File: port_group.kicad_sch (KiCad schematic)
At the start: 20 parts, among them U2 AOZ1268QI

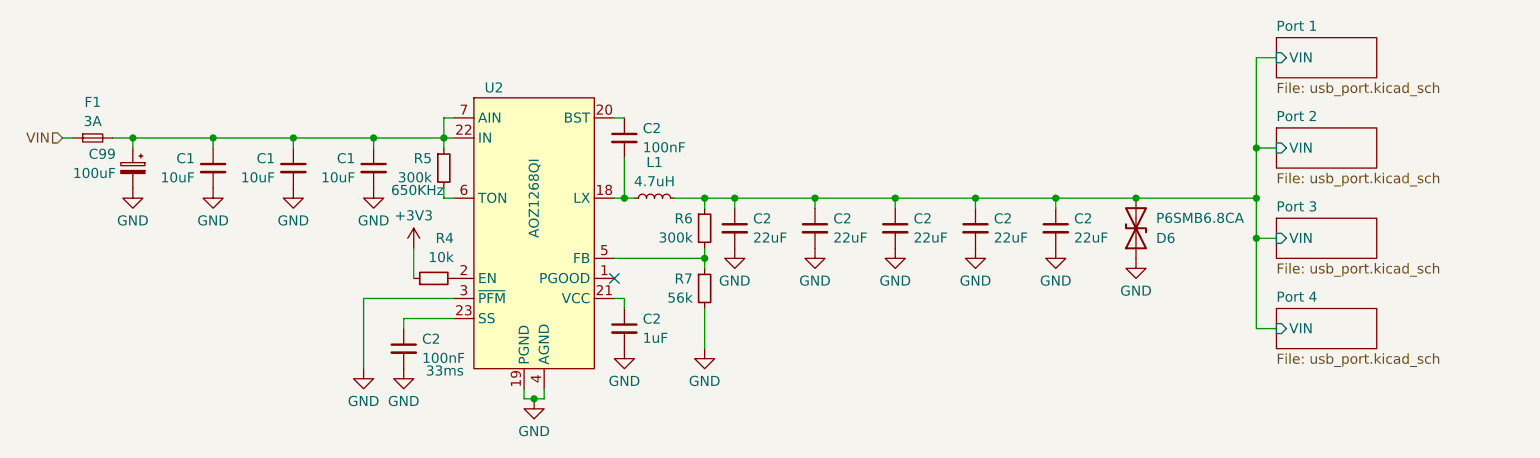
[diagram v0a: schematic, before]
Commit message: Add 5V auxiliary supply
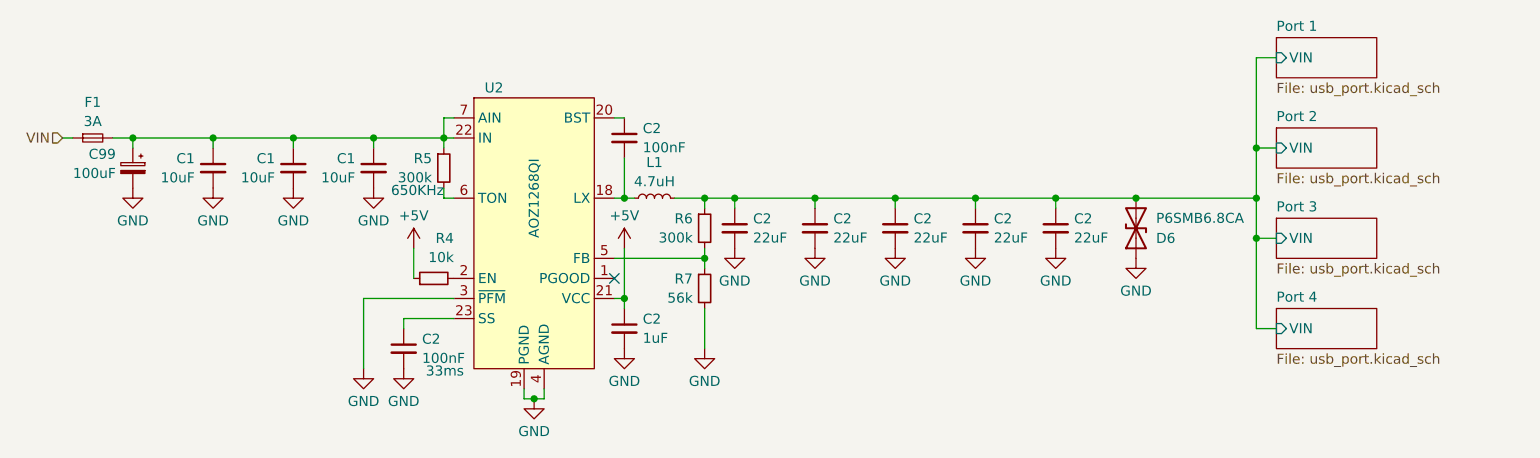
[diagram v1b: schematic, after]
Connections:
- net +3V3 is gone; now on net +5V: R4.1
- net +5V: now reaches C2.1, U2.21 (VCC)

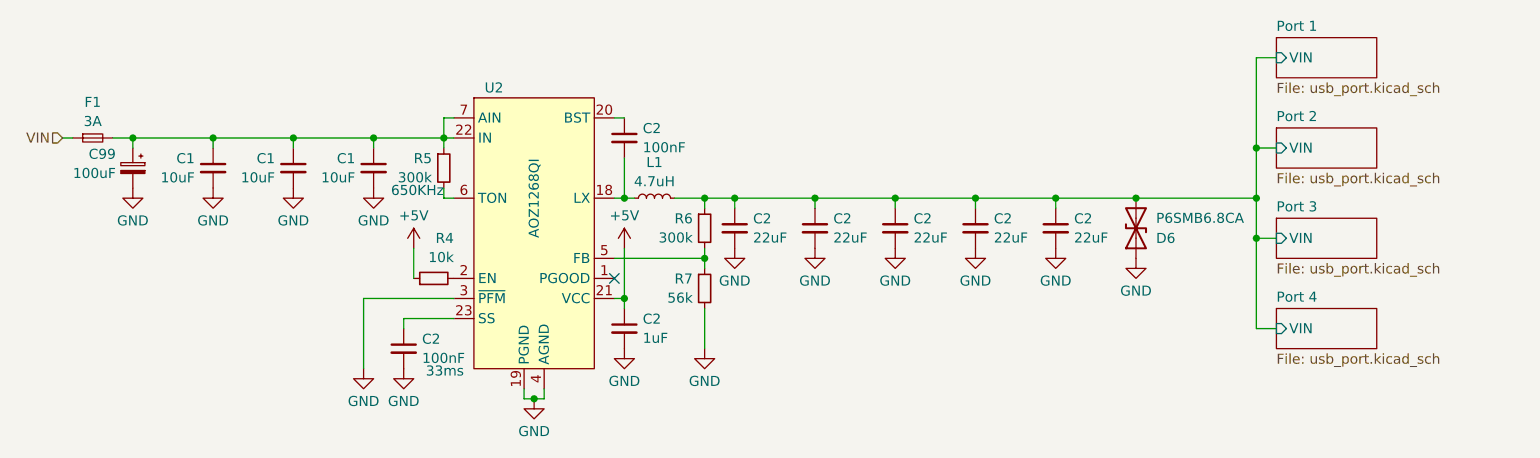
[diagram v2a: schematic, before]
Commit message: Do not populate buck converter VCC jumpers
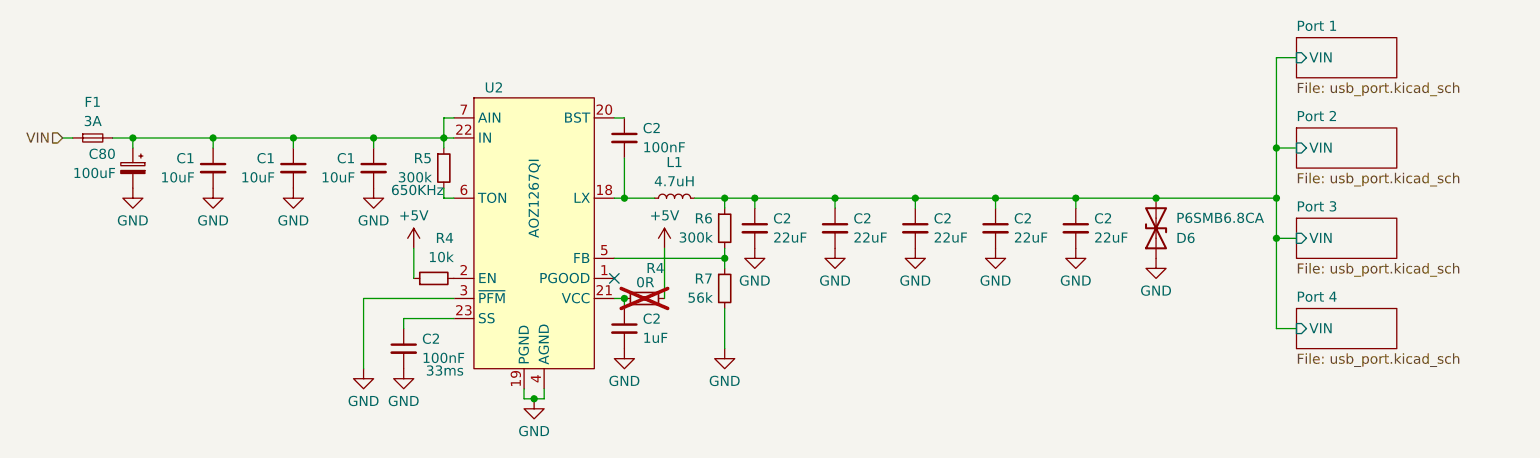
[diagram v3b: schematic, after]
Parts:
- added R4: 0R, Resistor_SMD:R_0402_1005Metric, symbol Device:R_Small
- U2: value AOZ1268QI -> AOZ1267QI
- renumbered C99 to C80
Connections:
- net +5V: now also R4.2; no longer C2.1, U2.21 (VCC)
- new net: C2.1, R4.1, U2.21 (VCC)
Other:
- moved on the sheet: C2, D6, L1, R6, R7
